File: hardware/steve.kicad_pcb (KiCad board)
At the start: 4 copper layers, 50 x 50 mm, 82 parts, among them Q1 Q_NMOS_GSD, Q2 Q_NMOS_GSD, Q3 Q_NMOS_GSD, Q4 Q_NMOS_GSD, Q5 Q_NMOS_GSD, Q6 Q_NMOS_GSD

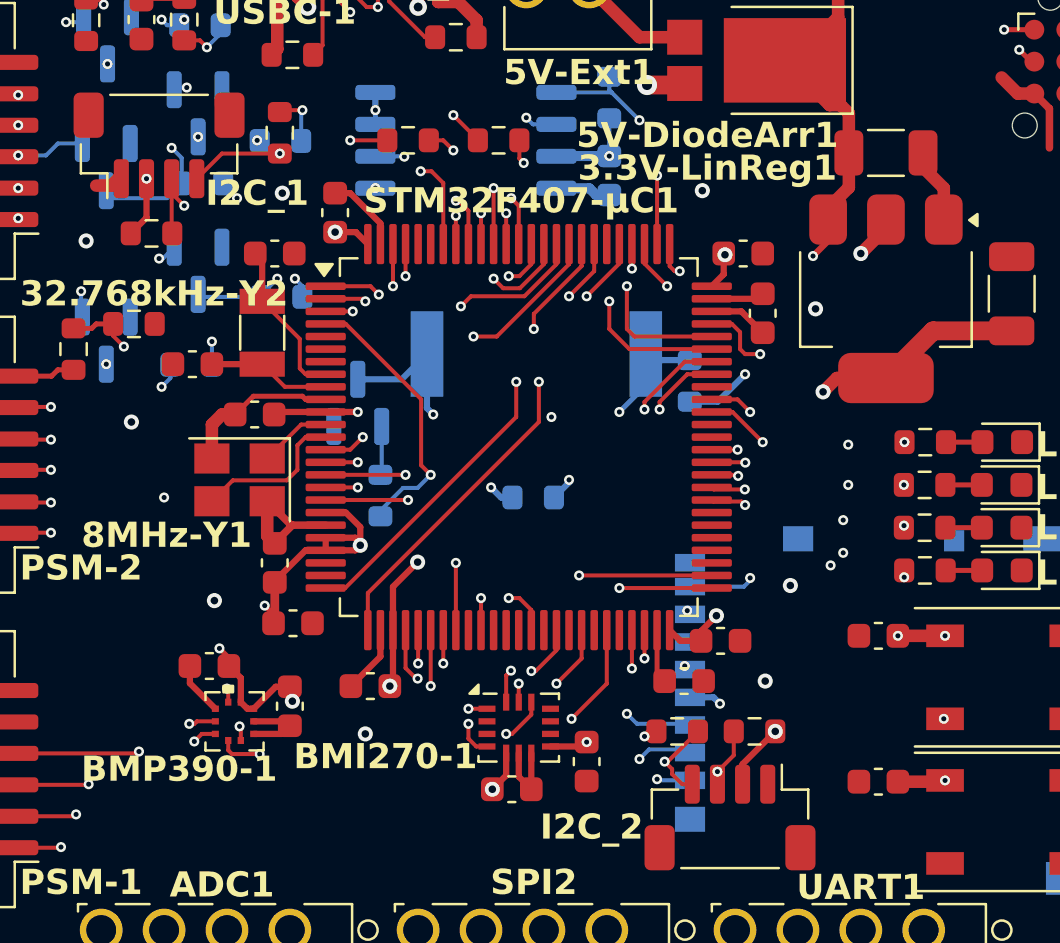
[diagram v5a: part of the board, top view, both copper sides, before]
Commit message: Added Custom Design Rules for JLC; fixed DRC errors
Added Custom Design Rules for JLC based on a community created custom ruleset.
Fixed DRC errors that the custom JLC rules pointed out. Updated project constraints to not throw extra errors.
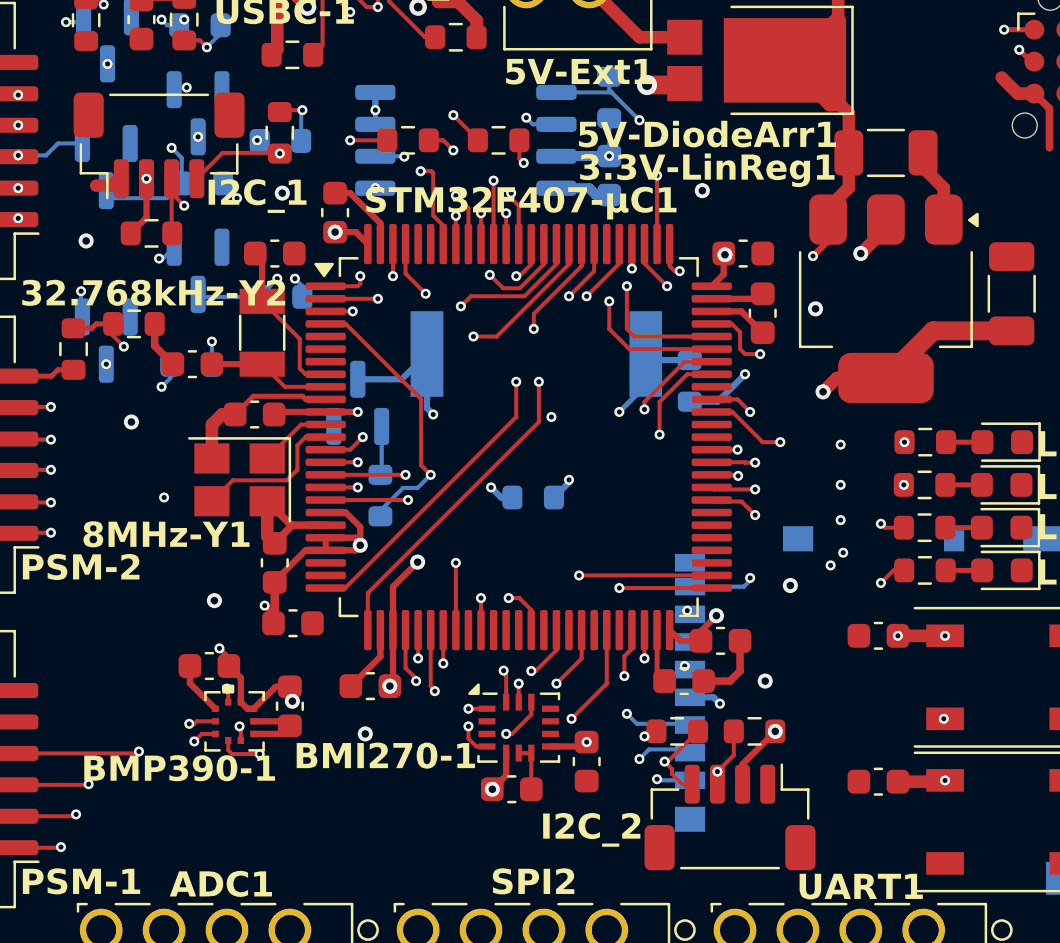
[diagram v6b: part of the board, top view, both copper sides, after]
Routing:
- net GND: track 50.9 -> 54.4 mm
- net MOSFET_3: track 20.0 -> 21.8 mm
- net MOSFET_4: track 18.1 -> 19.6 mm
- net MOSFET_1: track 21.8 -> 23.1 mm
- net MOSFET_2: track 20.8 -> 21.9 mm

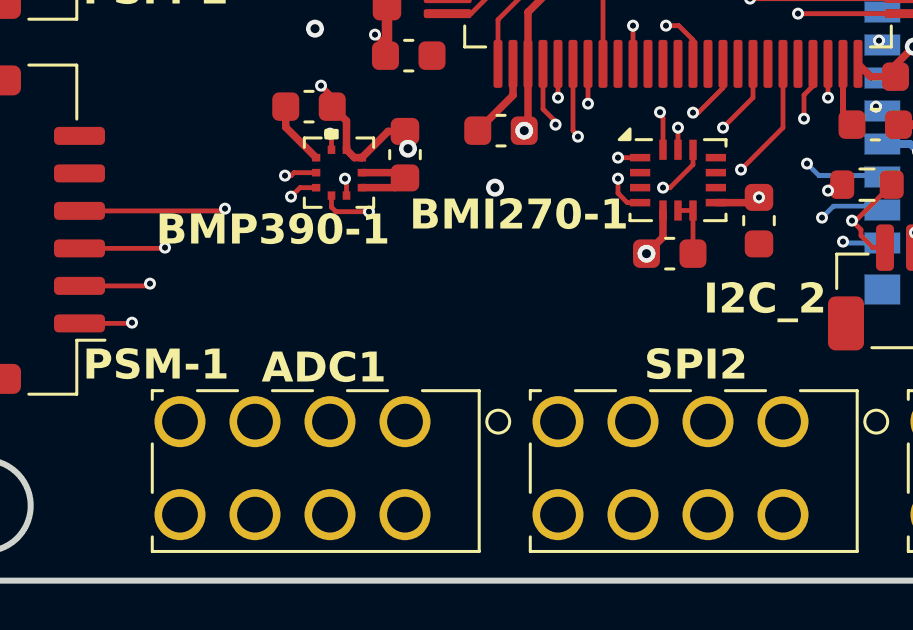
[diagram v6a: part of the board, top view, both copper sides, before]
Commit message: Add text to board
Add text to board silkscreen
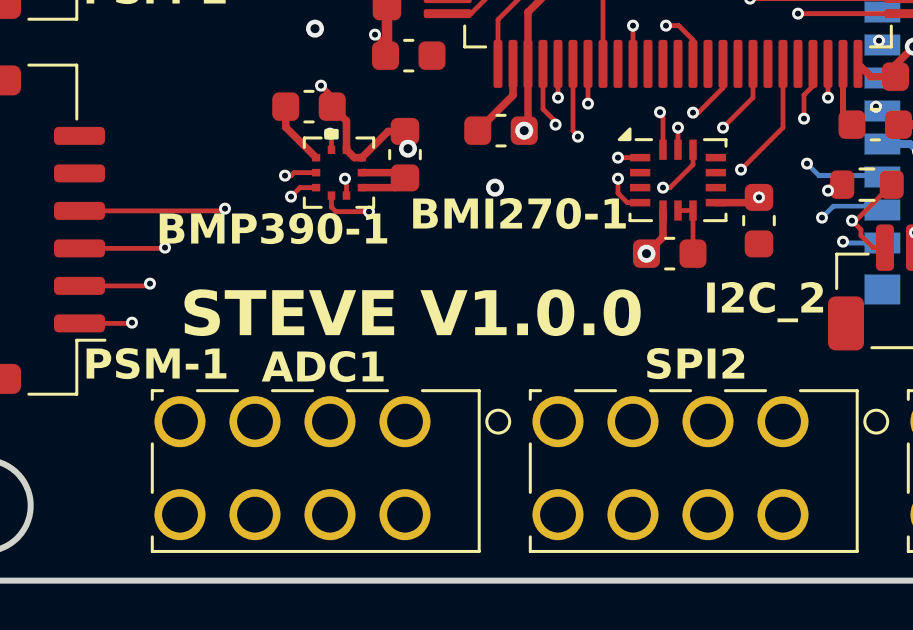
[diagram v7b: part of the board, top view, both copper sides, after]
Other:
- board text added: "STEVE V1.0.0"
- board text added: "{dblquote}Did you ever hear the tragedy of Darth Plagueis The Wise? I thought not. It's not a story the Jedi would tell you. It's a Sith legend. Darth Plagueis was a Dark Lord of the Sith, so powerful and so wise he could use the Force to influence the midichlorians to create life…{dblquote}"
- board text added: "{dblquote}I... am Steve{dblquote}"
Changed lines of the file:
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@@
 		(layer "F.CrtYd")
+	)
+	(gr_text "STEVE V1.0.0"
+		(at 109 142 0)
+		(layer "F.SilkS")
+		(effects
+			(font
+				(size 1.5 1.5)
+				(thickness 0.3)
+				(bold yes)
+			)
+			(justify left bottom)
+		)
+	)
+	(gr_text "{dblquote}I... am Steve{dblquote}"
+		(at 143.7 112.9 0)
+		(layer "B.SilkS")
+		(effects
+			(font
+				(size 1 1)
+				(thickness 0.15)
+			)
+			(justify left bottom mirror)
+		)
+	)
+	(gr_text "{dblquote}Did you ever hear the tragedy of Darth \nPlagueis The Wise? I thought not. It's \nnot a story the Jedi would tell you. It's \na Sith legend. Darth Plagueis was a \nDark Lord of the Sith, so powerful and \nso wise he could use the Force to \ninfluence the midichlorians to create \nlife…{dblquote}"
+		(at 131.1 141.9 0)
+		(layer "B.SilkS")
+		(effects
+			(font
+				(size 1 1)
+				(thickness 0.15)
+			)
+			(justify left bottom mirror)
+		)
 	)
 	(segment

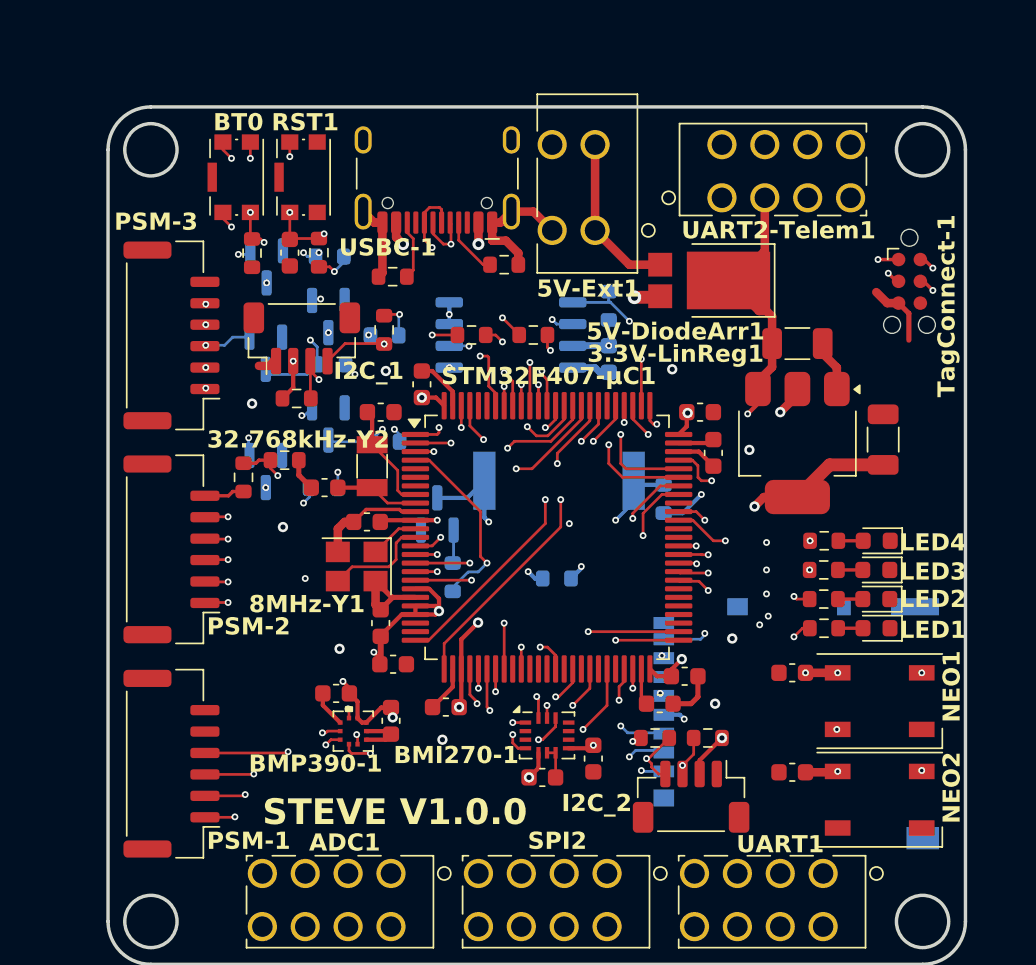
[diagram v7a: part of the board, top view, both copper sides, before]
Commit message: Schematic and Board fixes for Mfg
Schematic and Board fixes for Manufacturing. Added LCSC/JLC part numbers to values in schematic for BOM processing. Updated schematic fields. Added GND to each PSM connector. Brought PSM connector fix to PCB. Updated PCB designator locations from schematic changes.
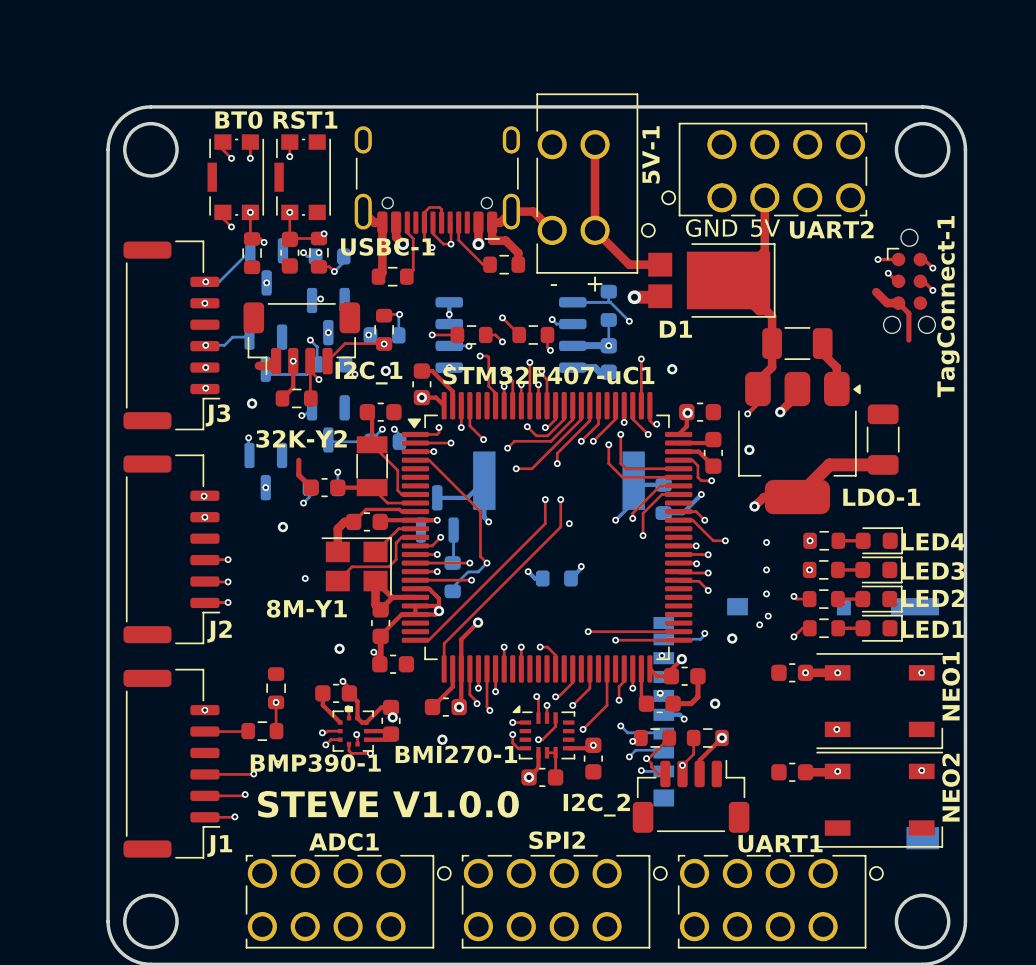
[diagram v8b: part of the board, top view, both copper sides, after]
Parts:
- 32K-Y2: renamed from 32.768kHz-Y2; value 32.768kHz -> 32.768kHz Crystal 12.5pf C90944
- 5V-1: renamed from 5V-Ext1; value TerminalBlock_1770885_2pos -> 5A Spring Conn 2pos C3818639
- 8M-Y1: renamed from 8MHz-Y1; value 8MHz -> 8MHz Crystal 10pf C400090
- ADC1, SPI2, UART1: value TerminalBlock_1770979_4pos_Vertical -> 5A Spring Conn 4pos C3818616
- BMI270-1: value BMI270 -> BMI270 Inertial Measurement Unit C2836813
- BMP390-1: value BMP390 -> BMP390 Barometric Pressure Sensor C2684802
- BT0, RST1: value KMR221G -> Button KMR221G C72443
- Buzzer1: value Speaker -> Externally Driven Buzzer 1.5-12.5V 4kHz 65dB C910763
- D1: renamed from 5V-DiodeArr1; value Schottky Diode Array, 5A per, 40V -> 10A/5A Schottky Diode Arr C780876
- Flash1: value W25Q128JVSIQ -> W25Q128JVSIQ 128Mb SPI Flash C97521
- I2C_1, I2C_2: value JST-SH-4P -> JST-SH-4P Vertical C160390
- J1: renamed from PSM-1; value PSM-Servo -> JST GH 6P Vertical 1A C189892
- J2: renamed from PSM-2; value PSM-MOSFET_BATT1 -> JST GH 6P Vertical 1A C189892
- J3: renamed from PSM-3; value PSM_Cont -> JST GH 6P Vertical 1A C189892
- LDO-1: renamed from 3.3V-LinReg1; value TLV1117LV33DCYR -> 3.3V 1A Lin Reg C15578
- NEO1, NEO2: value WS2812B -> WS2812B RGB LED C2761795
- Q1, Q2, Q3, Q4, Q5, Q6: value Q_NMOS_GSD -> NMOS GSD 350mA 60V C282405
- STM32F407-uC1: renamed from STM32F407-µC1; value STM32F407VGTx -> STM32F407VGTx Microcontroller C12345
- UART2: renamed from UART2-Telem1; value TerminalBlock_1770979_4pos_Vertical -> 5A Spring Conn 4pos C3818616
- USBC-1: value USB_C_Receptacle_16P -> USB-C Receptacle 16P C3025063
- uSD1: renamed from µSD1; value MicroSD_Hirose_DM3AT -> MicroSD Hirose DM3AT C114218
- moved R8 14.8 mm to (109.0, 136.4), turned to 180 degrees
- moved R9 13.3 mm to (109.8, 133.9), turned to -90 degrees
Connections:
- J1 pad 4: SERVO_PWM_4 -> GND
- J1 pad 5: unconnected-(PSM-1-Pin_5-Pad5) -> BATT1_V
- J1 pad 6: unconnected-(PSM-1-Pin_6-Pad6) -> SERVO_PWM_4
- J2 pad 4: MOSFET_4 -> GND
- J2 pad 5: MOSFET_5 -> MOSFET_4
- J2 pad 6: BATT1_V -> MOSFET_5
- J3 pad 4: CONT4_V_BATT -> GND
- J3 pad 5: CONT5_V_BATT -> CONT4_V_BATT
- J3 pad 6: unconnected-(PSM-3-Pin_6-Pad6) -> CONT5_V_BATT
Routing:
- net BATT1_V_ADC: track 22.4 -> 17.7 mm
- net SERVO_PWM_4: track 29.2 -> 31.2 mm, vias 2 -> 3
- net ADC_C1: track 33.6 -> 35.5 mm
- net CONT5_V_BATT: track 4.55 -> 3.40 mm, vias 2 -> 1
- net ADC_C0: track 29.4 -> 30.3 mm
- net MOSFET_4: track 19.6 -> 19.1 mm
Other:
- board text added: "+"
- board text added: "-"
- board text added: "5V"
- board text added: "GND"
